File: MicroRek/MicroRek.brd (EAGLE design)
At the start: 40 x 30 mm, 18 parts, among them IC3 LSM9DS1TR

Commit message: updated board layout
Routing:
- net MOSI3: track 21.5 -> 20.3 mm
- net SCK5: track 10.2 -> 11.3 mm
- net 3.3V: track 47.4 -> 48.0 mm
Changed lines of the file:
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@@
 <wire x1="8.6171" y1="4.67229375" x2="8.6171" y2="4.3944" width="0.4064" layer="16"/>
 <wire x1="8.6171" y1="4.3944" x2="10.3115" y2="2.7" width="0.4064" layer="16"/>
-<wire x1="22.72" y1="12.34" x2="22.27" y2="12.34" width="0.4064" layer="1"/>
+<wire x1="22.27" y1="12.34" x2="22.72" y2="12.34" width="0" layer="19" extent="1-16"/>
 <wire x1="11.375" y1="2.7" x2="9.9704" y2="1.2954" width="0.4064" layer="16"/>
 <wire x1="6.3246" y1="1.2954" x2="5.08" y2="2.54" width="0.4064" layer="16"/>
@@
 <contactref element="U$5" pad="P8"/>
 <contactref element="U$1" pad="P15"/>
-<wire x1="23.17" y1="12.39" x2="23.1348" y2="12.4252" width="0.3048" layer="1"/>
-<wire x1="23.1348" y1="12.4252" x2="23.1348" y2="12.86625" width="0.3048" layer="1"/>
-<wire x1="23.1348" y1="12.86625" x2="22.03105" y2="13.97" width="0.3048" layer="1"/>
-<wire x1="15.15" y1="13.97" x2="14.24" y2="13.06" width="0.3048" layer="1"/>
-<wire x1="22.03105" y1="13.97" x2="15.15" y2="13.97" width="0.3048" layer="1"/>
+<wire x1="14.24" y1="13.06" x2="16.42" y2="15.24" width="0.3048" layer="1"/>
+<wire x1="23.1348" y1="12.86625" x2="23.1348" y2="12.4252" width="0.3048" layer="1"/>
+<wire x1="23.1348" y1="12.4252" x2="23.17" y2="12.39" width="0.3048" layer="1"/>
+<wire x1="16.42" y1="15.24" x2="20.76105" y2="15.24" width="0.3048" layer="1"/>
+<wire x1="20.76105" y1="15.24" x2="23.1348" y2="12.86625" width="0.3048" layer="1"/>
 </signal>
 <signal name="MISO3">
@@
 <wire x1="11.65749375" y1="12.64250625" x2="11.65749375" y2="17.55250625" width="0.3048" layer="1"/>
 <via x="11.65749375" y="17.55250625" extent="1-16" drill="0.35"/>
-<wire x1="11.65749375" y1="17.55250625" x2="9.58749375" y2="17.55250625" width="0.3048" layer="16"/>
 <wire x1="5.02375" y1="24.1448" x2="4.8452" y2="23.96625" width="0.3048" layer="16"/>
-<wire x1="9.58749375" y1="17.55250625" x2="9.573" y2="17.567" width="0.3048" layer="16"/>
 <wire x1="5.42375" y1="21.6352" x2="5.5048" y2="21.6352" width="0.3048" layer="16"/>
 <wire x1="5.5048" y1="21.6352" x2="5.9" y2="21.24" width="0.3048" layer="16"/>
-<wire x1="9.573" y1="17.567" x2="9.573" y2="23.1429125" width="0.3048" layer="16"/>
 <wire x1="4.8452" y1="23.96625" x2="4.8452" y2="22.21375" width="0.3048" layer="16"/>
 <wire x1="4.8452" y1="22.21375" x2="5.42375" y2="21.6352" width="0.3048" layer="16"/>
 <wire x1="9.573" y1="23.1429125" x2="8.5711125" y2="24.1448" width="0.3048" layer="16"/>
 <wire x1="8.5711125" y1="24.1448" x2="5.02375" y2="24.1448" width="0.3048" layer="16"/>
+<wire x1="11.65749375" y1="17.55250625" x2="9.573" y2="19.637" width="0.3048" layer="16"/>
+<wire x1="9.573" y1="19.637" x2="9.573" y2="23.1429125" width="0.3048" layer="16"/>
 </signal>
 <signal name="SCK3">
@@
 <wire x1="12.1306" y1="24.99729375" x2="11.09289375" y2="26.035" width="0.4064" layer="1"/>
 <wire x1="11.09289375" y1="26.035" x2="9.525" y2="26.035" width="0.4064" layer="1"/>
-<wire x1="2" y1="7.54" x2="2.08" y2="7.62" width="0.3048" layer="16"/>
-<wire x1="2.08" y1="7.62" x2="5.08" y2="7.62" width="0.4064" layer="16"/>
 <wire x1="5.08" y1="7.62" x2="5.93" y2="8.47" width="0.4064" layer="16"/>
 <wire x1="5.93" y1="8.47" x2="5.93" y2="9.02" width="0.3048" layer="16"/>
@@
 <wire x1="4.5944" y1="19.38729375" x2="4.5944" y2="15.39270625" width="0.4064" layer="16"/>
 <wire x1="4.5944" y1="15.39270625" x2="5.7" y2="14.28710625" width="0.4064" layer="16"/>
-<wire x1="5.08" y1="7.62" x2="5.08" y2="6.5335" width="0.4064" layer="16"/>
+<wire x1="5.08" y1="7.62" x2="5.08" y2="7.112" width="0.4064" layer="16"/>
+<wire x1="5.08" y1="7.112" x2="5.08" y2="6.5335" width="0.4064" layer="16"/>
 <wire x1="5.08" y1="6.5335" x2="5.9885" y2="5.625" width="0.4064" layer="16"/>
 <wire x1="11.375" y1="7.3" x2="10.48" y2="7.3" width="0.4064" layer="16"/>
@@
 <wire x1="10.16" y1="7.62" x2="9.7994" y2="7.9806" width="0.4064" layer="1"/>
 <wire x1="9.7994" y1="7.9806" x2="7.62" y2="7.9806" width="0.4064" layer="1"/>
+<wire x1="2" y1="7.54" x2="4.652" y2="7.54" width="0.4064" layer="16"/>
+<wire x1="4.652" y1="7.54" x2="5.08" y2="7.112" width="0.4064" layer="16"/>
+<wire x1="4.652" y1="7.54" x2="5" y2="7.54" width="0.4064" layer="16"/>
+<wire x1="5" y1="7.54" x2="5.08" y2="7.62" width="0.4064" layer="16"/>
 </signal>
 <signal name="N$7">

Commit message: Updated MicroRek Board Layout
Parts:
- flipped C2 to the top
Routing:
- net 5V: track 24.3 -> 48.2 mm, vias 1 -> 4
- net SCK5: track 11.3 -> 13.6 mm
- net SCK3: track 9.60 -> 11.3 mm
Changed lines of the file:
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@@
 <elements>
 <element name="C1" library="resistor" library_urn="urn:adsk.eagle:library:348" package="C0402" package3d_urn="urn:adsk.eagle:package:26136/1" value="10uF" x="7" y="3" rot="MR0"/>
-<element name="C2" library="resistor" library_urn="urn:adsk.eagle:library:348" package="C0402" package3d_urn="urn:adsk.eagle:package:26136/1" value="" x="7" y="7" rot="MR0"/>
+<element name="C2" library="resistor" library_urn="urn:adsk.eagle:library:348" package="C0402" package3d_urn="urn:adsk.eagle:package:26136/1" value="" x="6.97" y="7"/>
 <element name="C3" library="resistor" library_urn="urn:adsk.eagle:library:348" package="C0402" package3d_urn="urn:adsk.eagle:package:26136/1" value="" x="5.28" y="9.02" rot="MR0"/>
 <element name="C4" library="resistor" library_urn="urn:adsk.eagle:library:348" package="C0402" package3d_urn="urn:adsk.eagle:package:26136/1" value="10nF" x="8.263" y="9.5" rot="R270"/>
@@
 <wire x1="6.595" y1="10.375" x2="6.595" y2="9.945" width="0" layer="19" extent="1-1"/>
 <wire x1="4.63" y1="9.02" x2="6.595" y2="10.375" width="0" layer="19" extent="1-1"/>
-<wire x1="6.35" y1="7" x2="4.63" y2="9.02" width="0" layer="19" extent="1-1"/>
-<wire x1="8.263" y1="8.85" x2="6.35" y2="7" width="0" layer="19" extent="1-1"/>
+<wire x1="7.62" y1="7" x2="4.63" y2="9.02" width="0" layer="19" extent="1-1"/>
+<wire x1="8.263" y1="8.85" x2="7.62" y2="7" width="0" layer="19" extent="1-1"/>
 <wire x1="6.35" y1="3" x2="8.263" y2="8.85" width="0" layer="19" extent="1-1"/>
 <wire x1="9.2" y1="13.29" x2="6.35" y2="3" width="0" layer="19" extent="1-1"/>
@@
 <wire x1="8.6171" y1="4.67229375" x2="8.6171" y2="4.3944" width="0.4064" layer="16"/>
 <wire x1="8.6171" y1="4.3944" x2="10.3115" y2="2.7" width="0.4064" layer="16"/>
-<wire x1="22.27" y1="12.34" x2="22.72" y2="12.34" width="0" layer="19" extent="1-16"/>
 <wire x1="11.375" y1="2.7" x2="9.9704" y2="1.2954" width="0.4064" layer="16"/>
 <wire x1="6.3246" y1="1.2954" x2="5.08" y2="2.54" width="0.4064" layer="16"/>
-<wire x1="5.08" y1="2.54" x2="5.08" y2="3.81" width="0.4064" layer="16"/>
+<wire x1="5.08" y1="3.3040875" x2="5.08" y2="3.81" width="0.4064" layer="16"/>
 <wire x1="5.08" y1="3.81" x2="5.645" y2="4.375" width="0.4064" layer="16"/>
 <wire x1="5.645" y1="4.375" x2="5.9885" y2="4.375" width="0.4064" layer="16"/>
 <wire x1="9.9704" y1="1.2954" x2="6.3246" y2="1.2954" width="0.4064" layer="16"/>
-<wire x1="21.37" y1="8.34" x2="22.27" y2="12.34" width="0" layer="19" extent="1-1"/>
-<wire x1="19.05" y1="3.81" x2="21.37" y2="8.34" width="0" layer="19" extent="1-16"/>
-<wire x1="7.65" y1="7" x2="8.0115" y2="5" width="0" layer="19" extent="16-16"/>
 <wire x1="11.375" y1="2.7" x2="12.7796" y2="1.2954" width="0.4064" layer="16"/>
 <wire x1="12.7796" y1="1.2954" x2="17.78" y2="1.2954" width="0.4064" layer="16"/>
@@
 <wire x1="19.05" y1="2.5654" x2="19.05" y2="3.81" width="0.4064" layer="16"/>
 <via x="19.05" y="3.81" extent="1-16" drill="0.35"/>
+<wire x1="19.05" y1="3.81" x2="19.05" y2="5.461" width="0.4064" layer="1"/>
+<wire x1="19.05" y1="5.461" x2="20.701" y2="7.112" width="0.4064" layer="1"/>
+<wire x1="20.701" y1="7.112" x2="21.37" y2="7.781" width="0.3048" layer="1"/>
+<wire x1="21.37" y1="7.781" x2="21.37" y2="8.34" width="0.3048" layer="1"/>
+<wire x1="19.05" y1="5.461" x2="19.05" y2="9.9718" width="0.4064" layer="1"/>
+<wire x1="19.05" y1="9.9718" x2="18.8894" y2="10.1324" width="0.4064" layer="1"/>
+<via x="18.8894" y="10.1324" extent="1-16" drill="0.35"/>
+<wire x1="18.8894" y1="10.1324" x2="18.8894" y2="11.8976" width="0.4064" layer="16"/>
+<via x="18.8894" y="11.8976" extent="1-16" drill="0.35"/>
+<wire x1="18.8894" y1="11.8976" x2="20.4538" y2="13.462" width="0.4064" layer="1"/>
+<wire x1="20.4538" y1="13.462" x2="21.209" y2="13.462" width="0.4064" layer="1"/>
+<wire x1="21.209" y1="13.462" x2="21.209" y2="13.401" width="0.3048" layer="1"/>
+<wire x1="21.209" y1="13.462" x2="21.6516" y2="13.0194" width="0.254" layer="1"/>
+<wire x1="21.6516" y1="13.0194" x2="22.04573125" y2="13.0194" width="0.254" layer="1"/>
+<wire x1="22.04573125" y1="13.0194" x2="22.27" y2="12.79513125" width="0.254" layer="1"/>
+<wire x1="22.27" y1="12.79513125" x2="22.27" y2="12.34" width="0.254" layer="1"/>
+<wire x1="22.04573125" y1="13.0194" x2="22.5406" y2="13.0194" width="0.254" layer="1"/>
+<wire x1="22.5406" y1="13.0194" x2="22.7382" y2="12.8218" width="0.254" layer="1"/>
+<wire x1="22.7382" y1="12.8218" x2="22.7382" y2="12.7" width="0.254" layer="1"/>
+<wire x1="22.7382" y1="12.7" x2="22.72" y2="12.6818" width="0.254" layer="1"/>
+<wire x1="22.72" y1="12.6818" x2="22.72" y2="12.34" width="0.254" layer="1"/>
+<wire x1="5.08" y1="3.81" x2="4.82704375" y2="3.55704375" width="0.4064" layer="16"/>
+<wire x1="4.82704375" y1="3.55704375" x2="4.06295625" y2="3.55704375" width="0.4064" layer="16"/>
+<via x="4.06295625" y="3.55704375" extent="1-16" drill="0.35"/>
+<wire x1="4.06295625" y1="3.55704375" x2="4.06295625" y2="4.74295625" width="0.4064" layer="1"/>
+<wire x1="4.06295625" y1="4.74295625" x2="6.32" y2="7" width="0.4064" layer="1"/>
+<wire x1="5.08" y1="2.54" x2="5.08" y2="3.3040875" width="0.4064" layer="16"/>
+<wire x1="5.08" y1="3.3040875" x2="4.82704375" y2="3.55704375" width="0.4064" layer="16"/>
 </signal>
 <signal name="N$2">
@@
 <contactref element="U$5" pad="P8"/>
 <contactref element="U$1" pad="P15"/>
-<wire x1="14.24" y1="13.06" x2="16.42" y2="15.24" width="0.3048" layer="1"/>
-<wire x1="23.1348" y1="12.86625" x2="23.1348" y2="12.4252" width="0.3048" layer="1"/>
-<wire x1="23.1348" y1="12.4252" x2="23.17" y2="12.39" width="0.3048" layer="1"/>
-<wire x1="16.42" y1="15.24" x2="20.76105" y2="15.24" width="0.3048" layer="1"/>
-<wire x1="20.76105" y1="15.24" x2="23.1348" y2="12.86625" width="0.3048" layer="1"/>
+<wire x1="23.17" y1="12.39" x2="23.17" y2="13.85839375" width="0.3048" layer="1"/>
+<wire x1="23.17" y1="13.85839375" x2="22.7816" y2="14.24679375" width="0.3048" layer="1"/>
+<wire x1="22.7816" y1="14.24679375" x2="22.7816" y2="15.24" width="0.3048" layer="1"/>
+<wire x1="22.7816" y1="15.24" x2="21.59" y2="16.4316" width="0.3048" layer="1"/>
+<wire x1="21.59" y1="16.4316" x2="21.59" y2="16.51" width="0.3048" layer="1"/>
+<wire x1="21.59" y1="16.51" x2="17.69" y2="16.51" width="0.3048" layer="1"/>
+<wire x1="17.69" y1="16.51" x2="14.24" y2="13.06" width="0.3048" layer="1"/>
 </signal>
 <signal name="MISO3">
@@
 <contactref element="U$3" pad="5"/>
 <contactref element="U$5" pad="P5"/>
-<wire x1="7.24921875" y1="19.04" x2="5.9" y2="19.04" width="0.3048" layer="16"/>
-<wire x1="12.74" y1="13.06" x2="12.59941875" y2="13.20058125" width="0.3048" layer="1"/>
-<wire x1="12.59941875" y1="13.20058125" x2="12.59941875" y2="13.6898" width="0.3048" layer="1"/>
-<via x="12.59941875" y="13.6898" extent="1-16" drill="0.35"/>
-<wire x1="12.59941875" y1="13.6898" x2="7.24921875" y2="19.04" width="0.3048" layer="16"/>
+<wire x1="12.74" y1="13.06" x2="12.74" y2="15.09941875" width="0.3048" layer="1"/>
+<wire x1="12.74" y1="15.09941875" x2="12.59941875" y2="15.24" width="0.3048" layer="1"/>
+<via x="12.59941875" y="15.24" extent="1-16" drill="0.35"/>
+<wire x1="8.79941875" y1="19.04" x2="5.9" y2="19.04" width="0.3048" layer="16"/>
+<wire x1="10.69158125" y1="15.827" x2="10.29149375" y2="16.2270875" width="0.3048" layer="16"/>
+<wire x1="10.29149375" y1="17.547925" x2="8.79941875" y2="19.04" width="0.3048" layer="16"/>
+<wire x1="10.29149375" y1="16.2270875" x2="10.29149375" y2="17.547925" width="0.3048" layer="16"/>
+<wire x1="12.59941875" y1="15.24" x2="12.01241875" y2="15.827" width="0.3048" layer="16"/>
+<wire x1="12.01241875" y1="15.827" x2="10.69158125" y2="15.827" width="0.3048" layer="16"/>
 </signal>
 <signal name="3.3V">

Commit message: LOTS of work on board layout
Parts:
- added LED1, LED2, LED3: (no value), led:CHIPLED_0805
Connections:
- removed net D2_5: U$1.P28
- removed net N$7: C7.1, IC3.P1, IC3.P3
- removed net VDD1: IC3.P22
- removed net VDD2: IC3.P23
- new net N$6: IC3.P22, IC3.P23
- net 3.3V: now also C7.1, IC3.P1, IC3.P3
- net D25: now also U$1.P28
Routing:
- net GND: track 0.00 -> 8.79 mm, vias 0 -> 7
- net N$7: track 5.38 -> 0.00 mm
- net 3.3V: track 48.0 -> 53.3 mm
- net SDA3: track 31.7 -> 34.9 mm

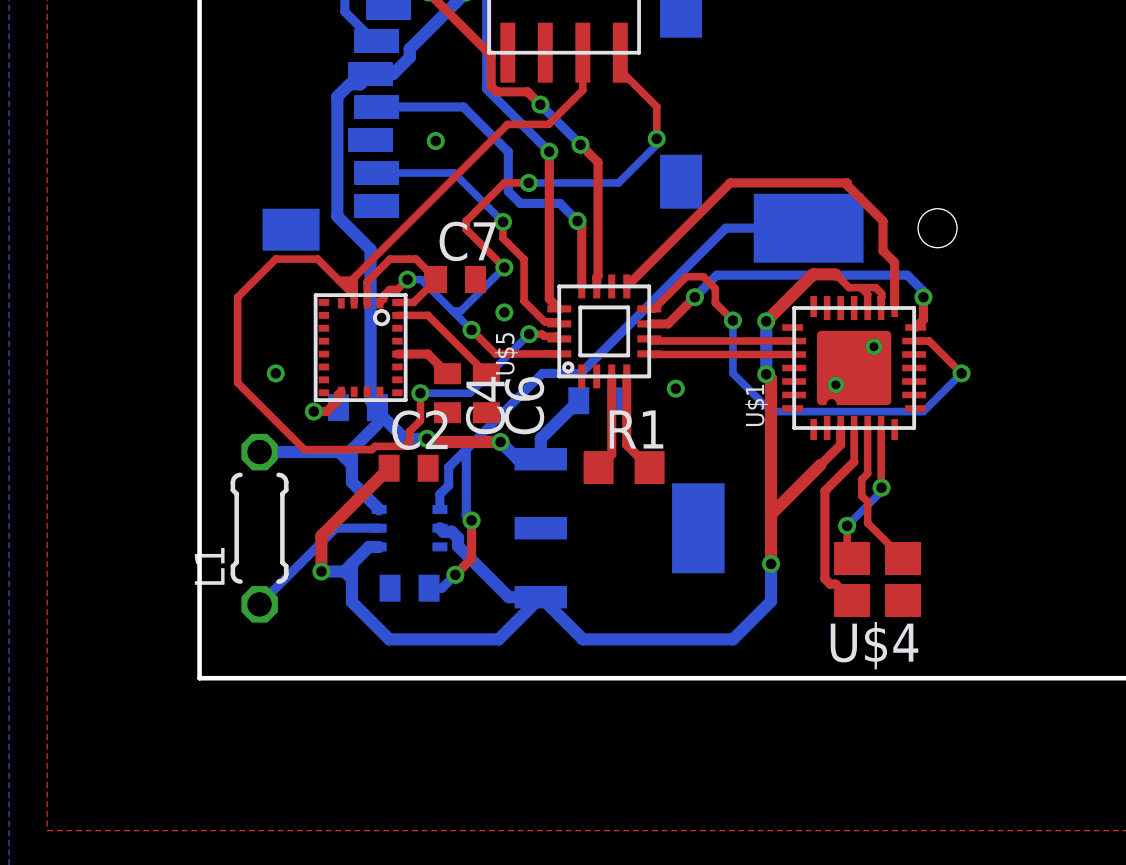
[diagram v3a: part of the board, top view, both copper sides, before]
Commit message: MicroRek Updates
Changed inductor package
Fixed some wiring
Fixed Crystal wiring (MAYBE)
Will work more in the morning
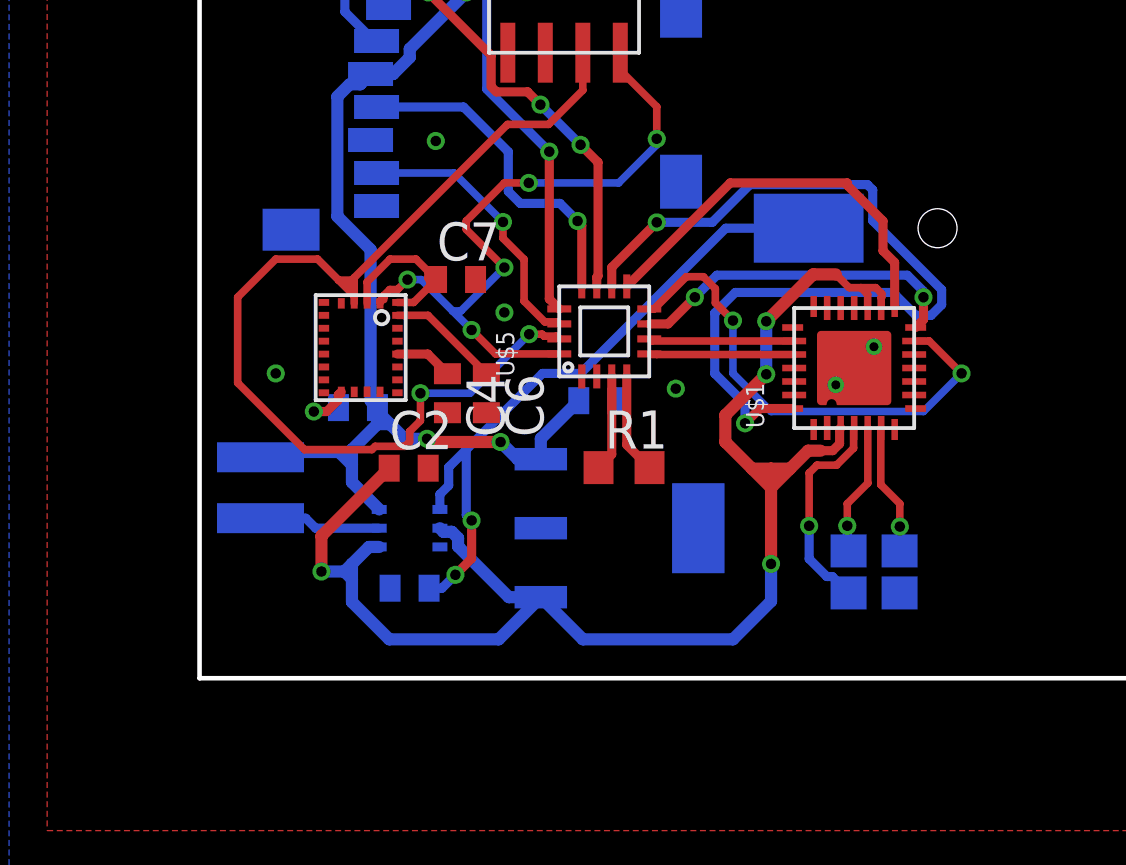
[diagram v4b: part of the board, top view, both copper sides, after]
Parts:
- L1: device resistor:0204/5 -> CPSS:MICROREK_INDUCTOR
- moved L1 1.35 mm to (2.03, 6.35), flipped to the bottom
- moved U$4 0.28 mm to (22.5, 3.54), flipped to the bottom
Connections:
- net 3.3V: now also L1.P$2; no longer L1.2
- net N$3: now also L1.P$1; no longer L1.1
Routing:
- net D25: track 0.00 -> 29.5 mm, vias 0 -> 2
- net 5V: track 48.2 -> 51.3 mm
- net N$3: track 5.04 -> 4.10 mm
- net CPB6: track 5.00 -> 4.40 mm, vias 0 -> 1
- net CPB7: track 4.90 -> 4.37 mm, vias 2 -> 1
- net GND: track 8.79 -> 9.31 mm, vias 7 -> 8

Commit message: Board Updates
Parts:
- added R2: 100Ω, resistor:R0603
- added R3: 100kΩ, resistor:R0603
- added R4: 4.7kΩ, resistor:R0603
- added R5, R6, R7, R8: 10kΩ, resistor:R0603
- moved U$4 5.97 mm to (28.3, 2.27), flipped to the top
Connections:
- net 3.3V: now also IC3.P22, IC3.P23, R4.1
- net 5V: now also R5.2, R6.2, R7.1, R8.1
- net CPB6: now also U$4.2; no longer U$4.1
- net CPB7: now also U$4.4; no longer U$4.2
- net GND: now also R2.1, R2.2, R3.1, R4.2, U$4.1; no longer U$4.4
- net N$6: now also LED1.C, R3.2; no longer IC3.P22, IC3.P23
- net SCL3: now also R8.2
- net SCL5: now also R6.1
- net SDA3: now also R7.2
- net SDA5: now also R5.1
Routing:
- net CPB6: track 4.40 -> 15.9 mm, vias 1 -> 0
- net CPB7: track 4.37 -> 15.5 mm, vias 1 -> 0
- net GND: track 9.31 -> 16.1 mm

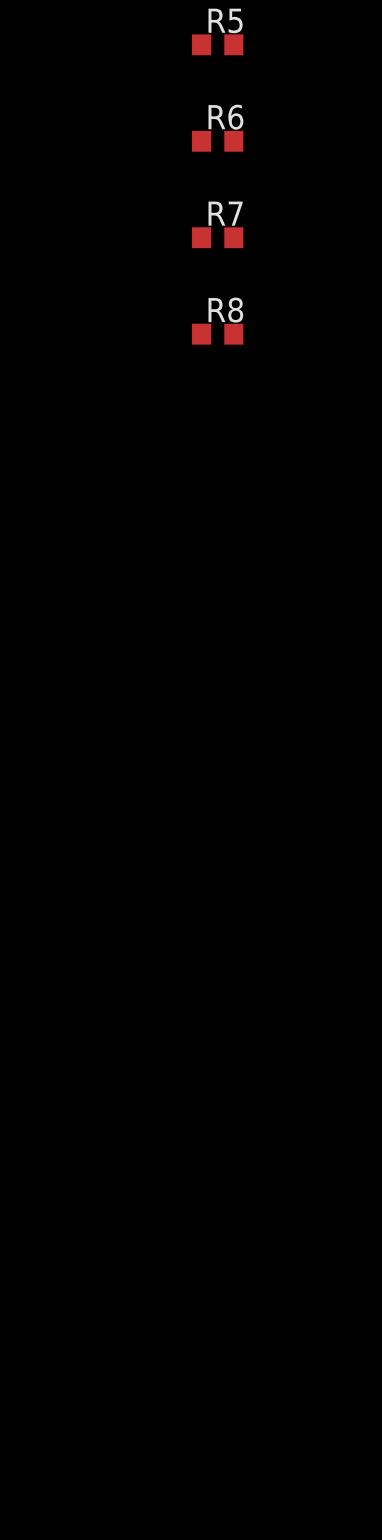
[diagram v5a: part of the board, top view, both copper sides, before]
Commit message: MicroRek Update
Added pullup resistors and the mini icsp port
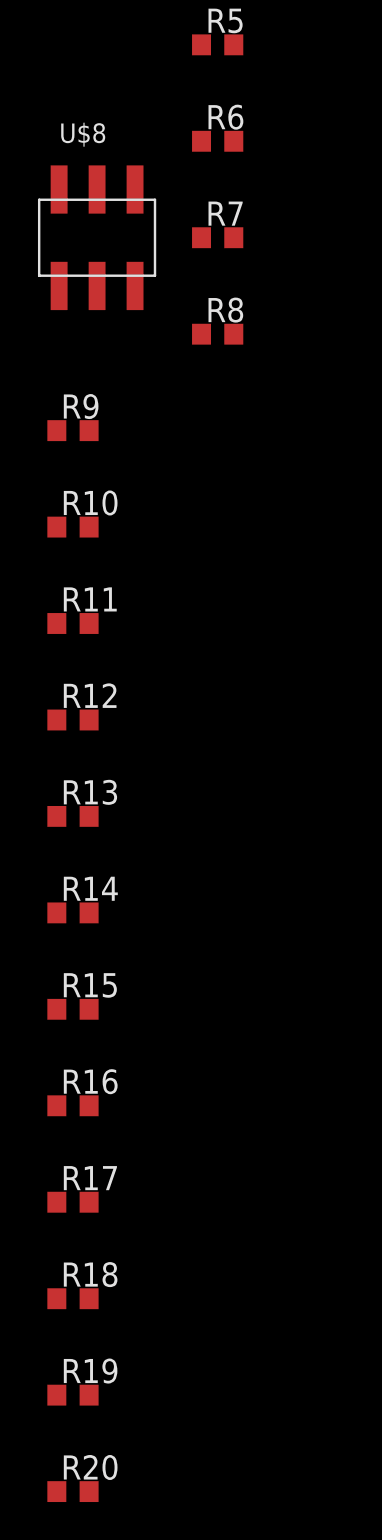
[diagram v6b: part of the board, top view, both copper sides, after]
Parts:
- added R10, R11, R12, R13, R14, R15, R16, R17, R18, R19, R20, R9: 4.7kΩ, resistor:R0603
- added U$8: MINI_ICSP, CPSS_CONNECTOR:NPNN032FFKS-RC
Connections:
- net 3.3V: now also R15.1, R16.1, R17.1, R18.1, R19.1, R20.1, U$8.VCC
- net 5V: now also R10.2, R11.2, R12.2, R13.2, R14.2, R9.2
- net D23: now also R16.2
- net D25: now also R9.1
- net GND: now also U$8.GND
- net MISO3: now also R19.2, U$8.MISO
- net MISO5: now also R12.1
- net MOSI3: now also R18.2, U$8.MOSI
- net MOSI5: now also R11.1
- net RESET: now also U$8.RST
- net SCK3: now also R17.2, U$8.SCK
- net SCK5: now also R10.1
- net SCL3: now also R15.2
- net SCL5: now also R14.1
- net SDA3: now also R20.2
- net SDA5: now also R13.1
